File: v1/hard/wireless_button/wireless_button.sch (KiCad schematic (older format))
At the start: 34 parts, among them J1 USB_B_Micro, J2 RJ12, J3 Conn_01x01_Female, J4 Conn_01x06_Male, Q1 Q_PMOS_GSD, SW1 SW_Push, U1 STM32F103C8Tx, U2 CC1101_MOD, U3 OLED_0.91, U4 24LC128, Y1 8MHz

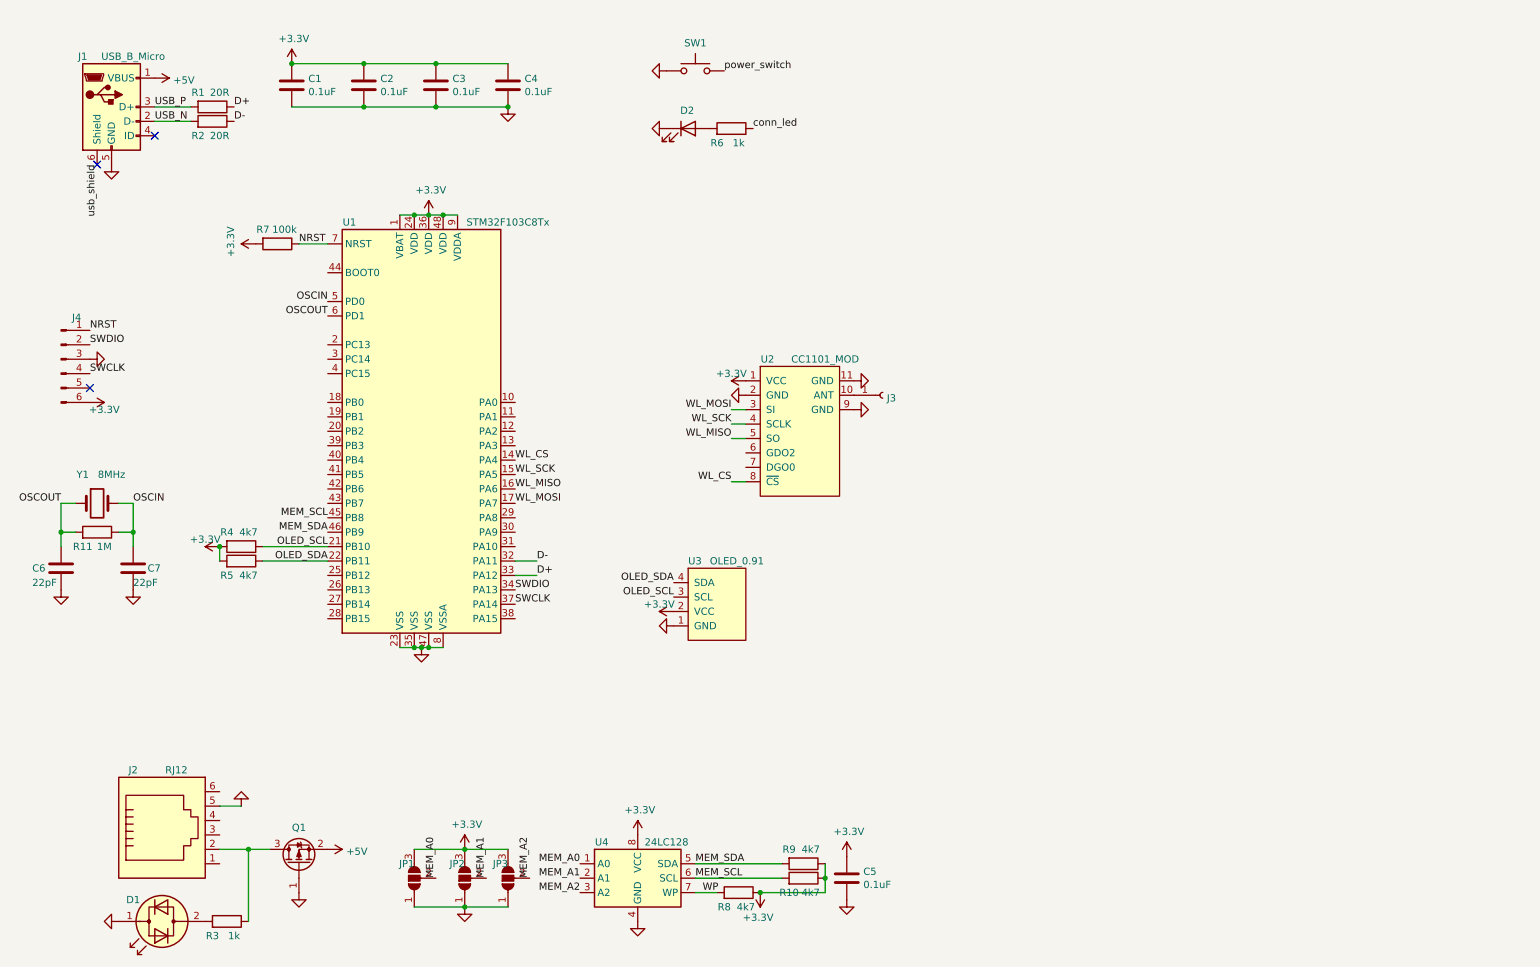
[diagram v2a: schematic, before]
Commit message: Finished wireless button PCB v0.1. Added step-down converter to 3.3V from wide range input voltage. May contain serios mistakes, board is a prototype only.
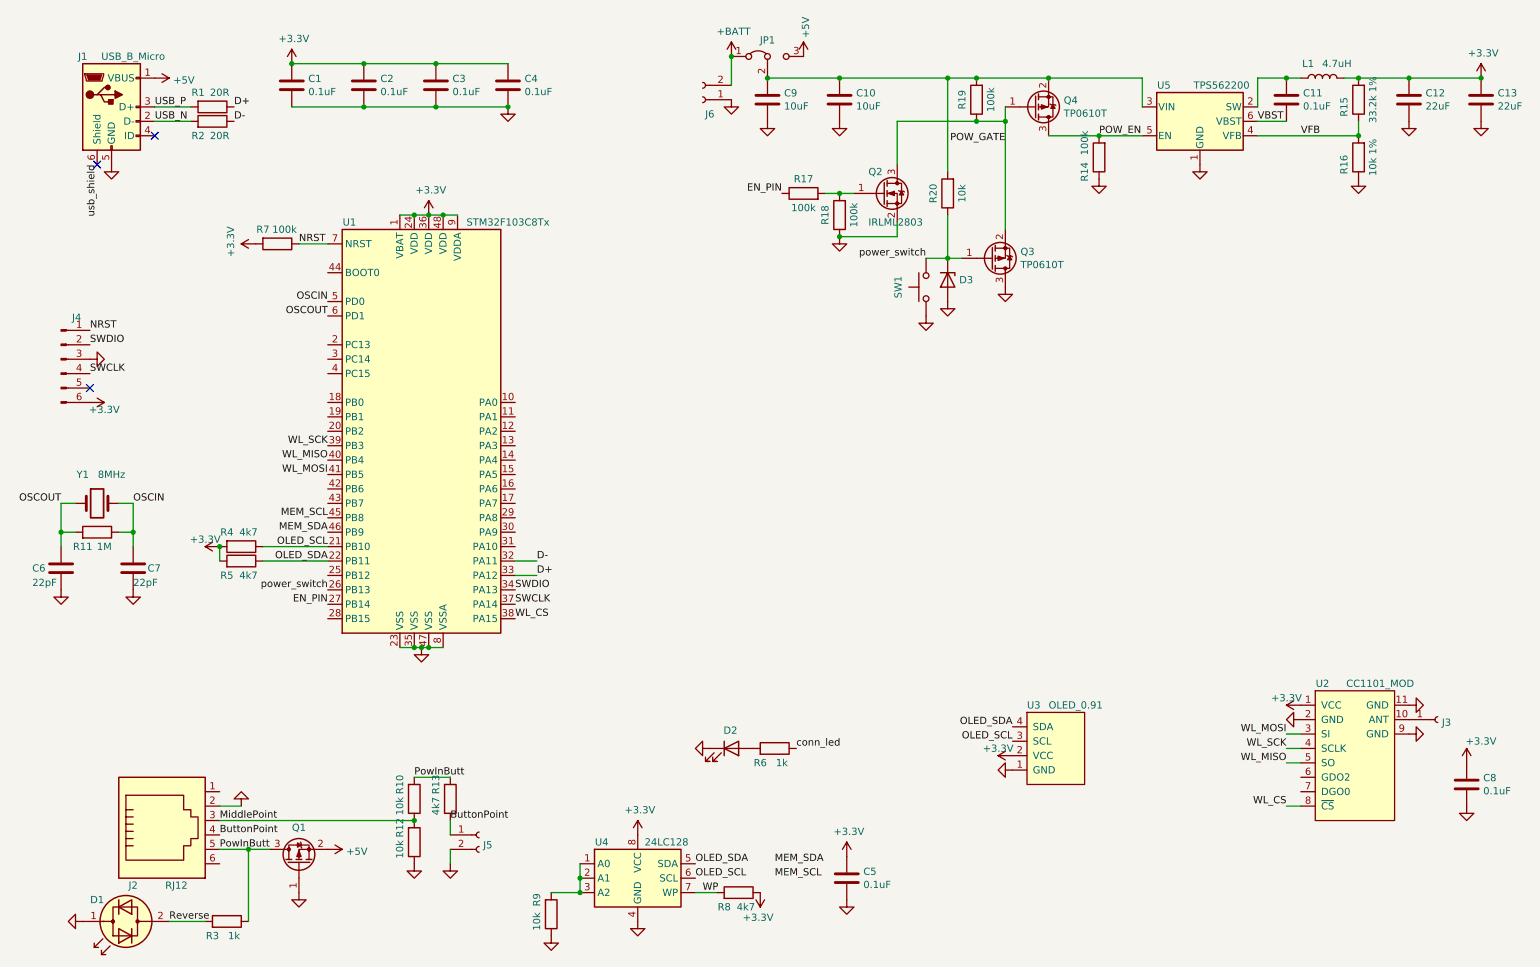
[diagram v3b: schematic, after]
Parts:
- removed JP1: A0, Jumper:SolderJumper-3_P2.0mm_Open_TrianglePad1.0x1.5mm, symbol Jumper:SolderJumper_3_Open
- removed JP2: A1, Jumper:SolderJumper-3_P2.0mm_Open_TrianglePad1.0x1.5mm, symbol Jumper:SolderJumper_3_Open
- removed JP3: A2, Jumper:SolderJumper-3_P2.0mm_Open_TrianglePad1.0x1.5mm, symbol Jumper:SolderJumper_3_Open
- added C10, C9: 10uF, Resistor_SMD:R_0805_2012Metric_Pad1.15x1.40mm_HandSolder, symbol Device:C
- added C11, C8: 0.1uF, Resistor_SMD:R_0805_2012Metric_Pad1.15x1.40mm_HandSolder, symbol Device:C
- added C12, C13: 22uF, Resistor_SMD:R_0805_2012Metric_Pad1.15x1.40mm_HandSolder, symbol Device:C
- added D3: 4.8V, Diode_SMD:D_SOD-123, symbol Device:D_Zener
- added J5: Conn_01x02_Female, Connector_PinSocket_2.54mm:PinSocket_1x02_P2.54mm_Vertical, symbol Connector:Conn_01x02_Female
- added J6: Conn_01x02_Female, brbuttonsystem:Wago 250-3.5-2P-2, symbol Connector:Conn_01x02_Female
- added JP1: Jumper_3_Bridged12, Jumper:SolderJumper-3_P2.0mm_Open_TrianglePad1.0x1.5mm, symbol Jumper:Jumper_3_Bridged12
- added L1: 4.7uH, Inductor_SMD:L_Taiyo-Yuden_NR-60xx_HandSoldering, symbol Device:L
- added Q2: IRLML2803, Package_TO_SOT_SMD:SOT-23, symbol Transistor_FET:IRLML2060
- added Q3, Q4: TP0610T, Package_TO_SOT_SMD:SOT-23, symbol Transistor_FET:TP0610T
- added R12, R20: 10k, Resistor_SMD:R_0805_2012Metric_Pad1.15x1.40mm_HandSolder, symbol Device:R
- added R13: 4k7, Resistor_SMD:R_0805_2012Metric_Pad1.15x1.40mm_HandSolder, symbol Device:R
- added R14, R17, R18, R19: 100k, Resistor_SMD:R_0805_2012Metric_Pad1.15x1.40mm_HandSolder, symbol Device:R
- added R15: 33.2k 1%, Resistor_SMD:R_0805_2012Metric_Pad1.15x1.40mm_HandSolder, symbol Device:R
- added R16: 10k 1%, Resistor_SMD:R_0805_2012Metric_Pad1.15x1.40mm_HandSolder, symbol Device:R
- added U5: TPS562200, Package_TO_SOT_SMD:SOT-23-6, symbol Regulator_Switching:TPS562200
- R10, R9: value 4k7 -> 10k
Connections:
- net MEM_A1 is gone; now on an unnamed net: U4.2 (A1)
- net MEM_A2 is gone; now on an unnamed net: U4.3 (A2)
- net +3V3: now also C12.1, C13.1, C8.1, L1.2, R15.2; no longer R10.1, R9.1
- net +5V: now also JP1.3 (B)
- net GND: now also J2.2, R9.1, C10.2, C12.2, C13.2, C8.2, C9.2, D3.2 (A), J5.2 (Pin_2), J6.1 (Pin_1), Q2.2 (S), Q3.3 (D), R12.1, R14.1, R16.1, R18.1, U5.1 (GND); no longer J2.5
- net MEM_SCL: no longer R10.2, U4.6 (SCL)
- net MEM_SDA: no longer R9.2, U4.5 (SDA)
- net OLED_SCL: now also U4.6 (SCL)
- net OLED_SDA: now also U4.5 (SDA)
- net WL_CS: now also U1.38 (PA15); no longer U1.14 (PA4)
- net WL_MISO: now also U1.40 (PB4); no longer U1.16 (PA6)
- net WL_MOSI: now also U1.41 (PB5); no longer U1.17 (PA7)
- net WL_SCK: now also U1.39 (PB3); no longer U1.15 (PA5)
- net power_switch: now also U1.26 (PB13), D3.1 (K), Q3.1 (G), R20.1
- net EN_PIN: now reaches U1.27 (PB14)
- net EN_PIN: now also R17.1
- net PowInButt: now reaches Q1.3 (D), R3.1
- net PowInButt: now also J2.5, R10.2, R13.2; no longer J2.2
- net MiddlePoint: now reaches J2.3
- net MiddlePoint: now also R10.1, R12.2
- net ButtonPoint: now reaches J2.4
- net ButtonPoint: now also J5.1 (Pin_1), R13.1
- net Reverse: now reaches D1.2 (AK), R3.2
- net MEM_A0: no longer names the net of U4.1 (A0)
- net MEM_A0: now also R9.2
- new net: C11.1, L1.1, U5.2 (SW)
- new net: C10.1, C9.1, JP1.2 (C), Q4.2 (S), R19.2, R20.2, U5.3 (VIN)
- new net: Q2.1 (G), R17.2, R18.2
- new net +BATT: J6.2 (Pin_2), JP1.1 (A)
- new net POW_EN: Q4.3 (D), R14.2, U5.5 (EN)
- new net POW_GATE: Q2.3 (D), Q3.2 (S), Q4.1 (G), R19.1
- new net VBST: C11.2, U5.6 (VBST)
- new net VFB: R15.1, R16.2, U5.4 (VFB)
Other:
- moved on the sheet: D1, D2, J3, R6, SW1, U2, U3
